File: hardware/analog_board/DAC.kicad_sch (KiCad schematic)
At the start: 120 parts, among them Q1 MMBT3906, Q2 MMBT3906, U3 AD9747BCPZ, U4 OPA695ID, U5 OPA695ID, U6 NE5532

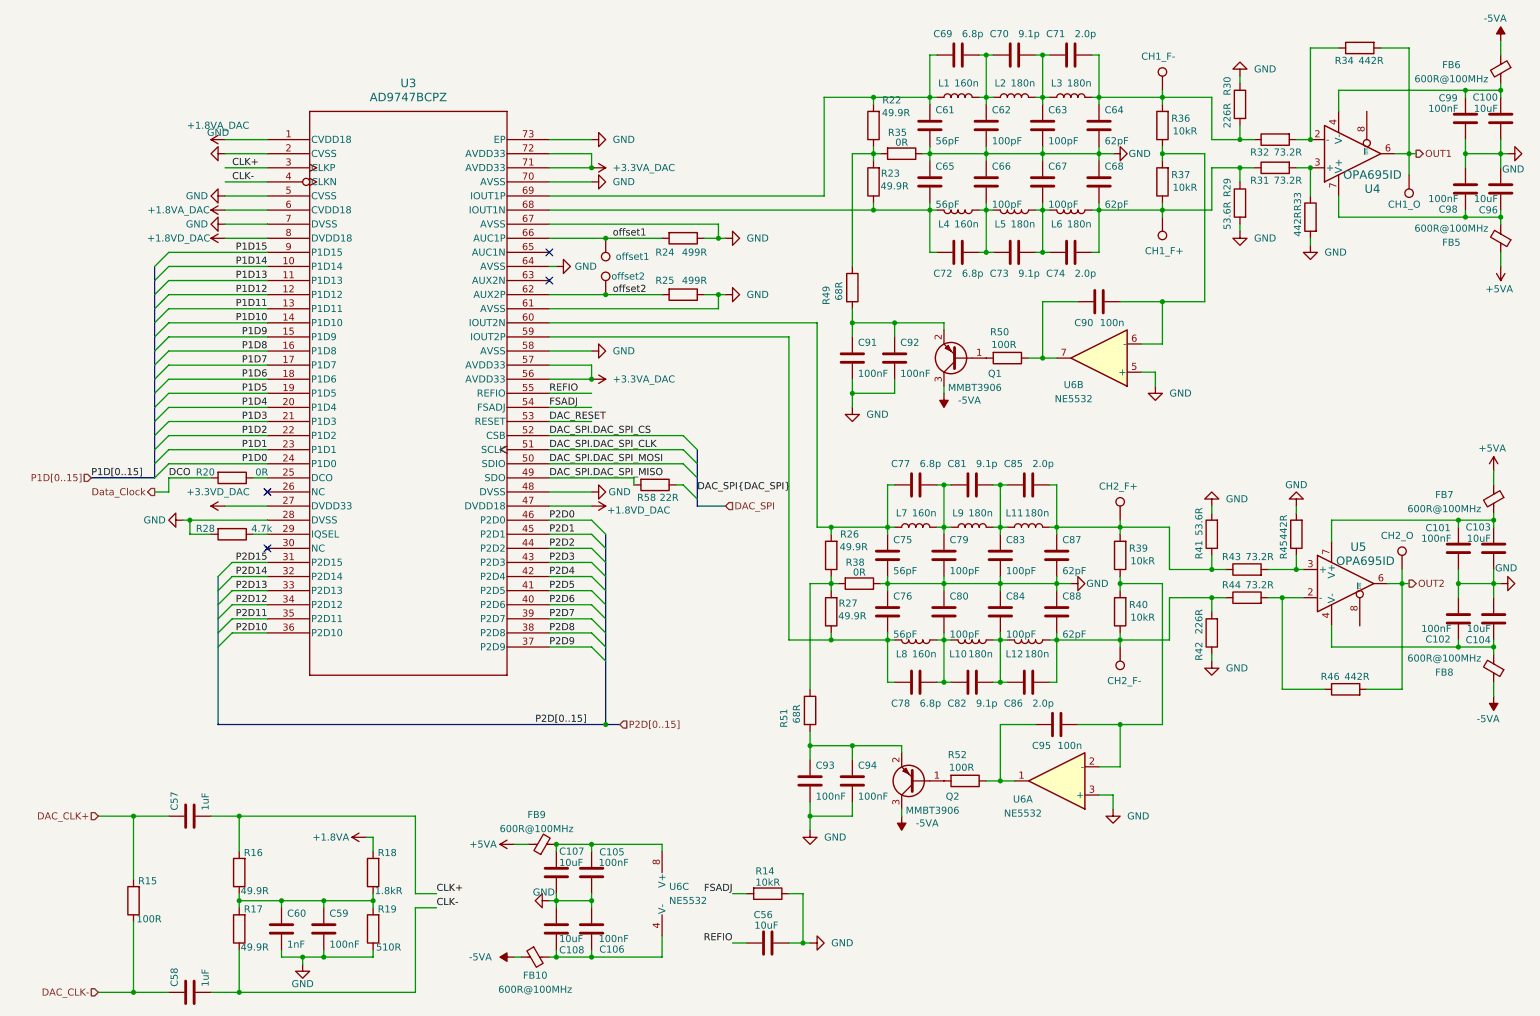
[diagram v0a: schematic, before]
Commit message: feat：根据PCB微调原理图
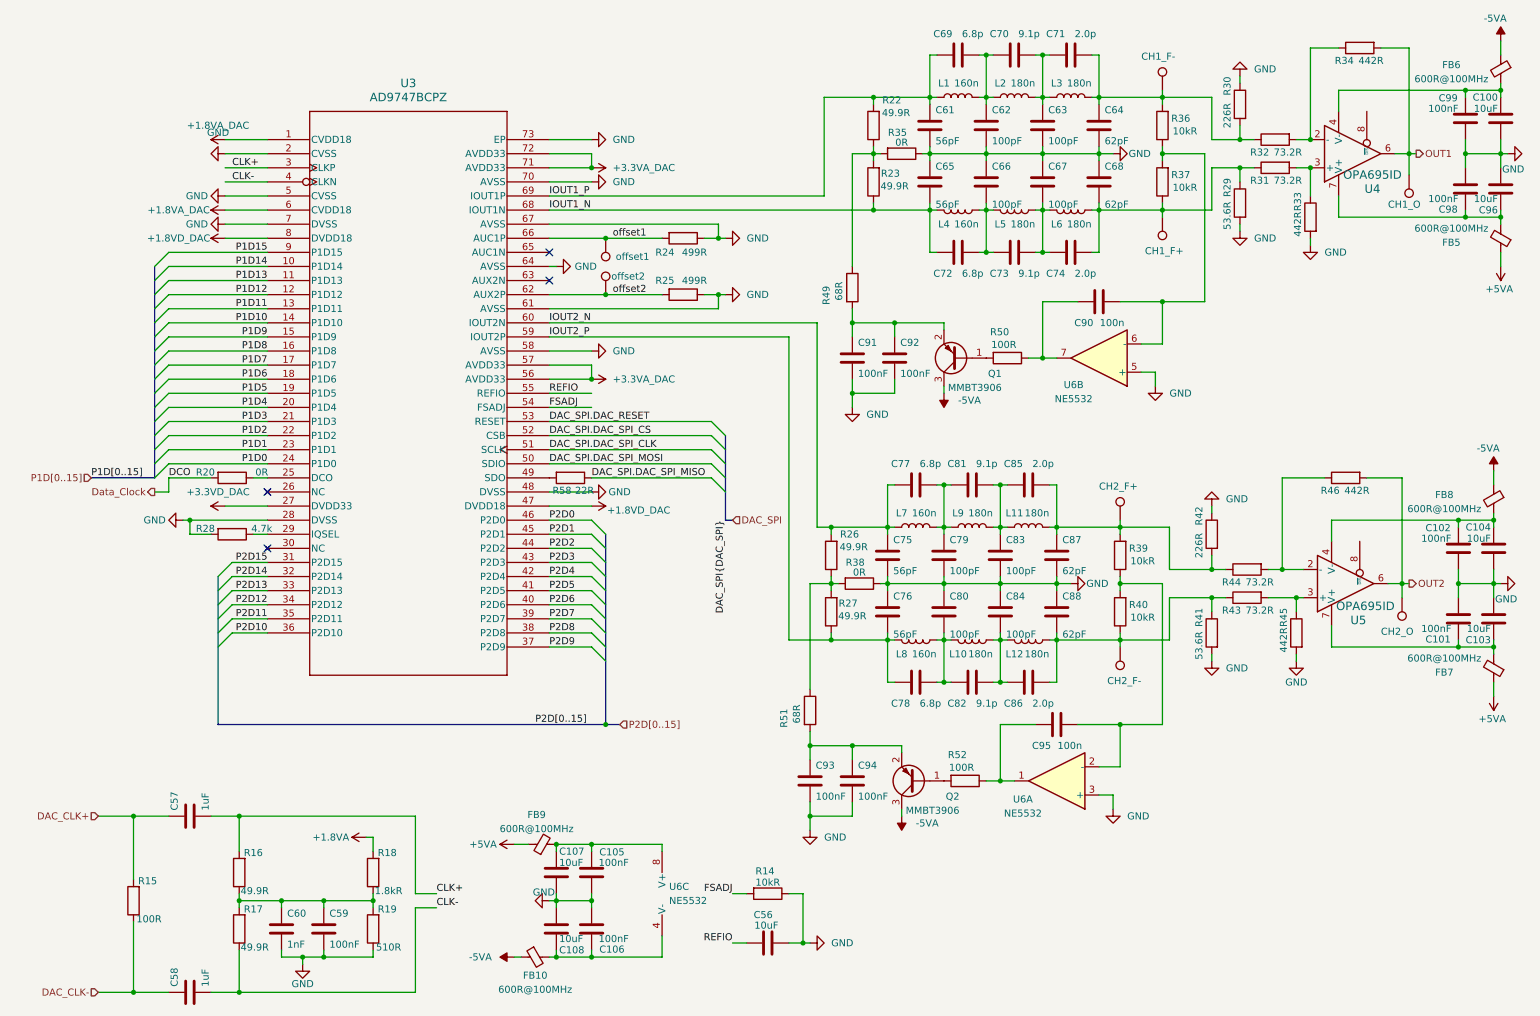
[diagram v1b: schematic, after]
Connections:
- net DAC_SPI.DAC_SPI_MISO: now also R58.1; no longer R58.2, U3.49 (SDO)
- net IOUT2_P: now reaches C76.1, C78.2, L8.1, R27.1, U3.59 (IOUT2P)
- net IOUT2_N: now reaches C75.2, C77.2, L7.1, R26.2, U3.60 (IOUT2N)
- net IOUT1_N: now reaches C65.1, C72.2, L4.1, R23.1, U3.68 (IOUT1N)
- net IOUT1_P: now reaches C61.2, C69.2, L1.1, R22.2, U3.69 (IOUT1P)
- net at C85.1, C87.2, L11.2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: now also R42.2, R44.1; no longer R41.1, R43.1
- net at C86.1, C88.1, L12.2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: now also R41.1, R43.1; no longer R42.2, R44.1
- net DAC_RESET renamed DAC_SPI.DAC_RESET
- new net: R58.2, U3.49 (SDO)
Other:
- moved on the sheet: R58

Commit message: feat：添加平衡铜
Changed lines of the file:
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@@
 		(in_pos_files yes)
 		(dnp no)
-		(fields_autoplaced yes)
 		(property "Reference" "#PWR049"
 			(at 53.34 39.37 0)
@@
 		)
 		(property "Value" "+1.8VA_DAC"
-			(at 48.26 36.83 90)
+			(at 41.148 39.116 90)
 			(show_name no)
 			(do_not_autoplace no)
@@
 		(in_pos_files yes)
 		(dnp no)
-		(fields_autoplaced yes)
 		(property "Reference" "#PWR032"
 			(at 43.18 41.91 0)
@@
 		)
 		(property "Value" "GND"
-			(at 48.26 38.1 90)
+			(at 44.704 41.91 90)
 			(show_name no)
 			(do_not_autoplace no)

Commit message: feat：导出模拟板 BOM
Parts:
- TP1, TP2, TP3, TP4, TP5, TP6, TP7, TP8: now left out of the parts list
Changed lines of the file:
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@@
 		(body_style 1)
 		(exclude_from_sim no)
-		(in_bom yes)
+		(in_bom no)
 		(on_board yes)
 		(in_pos_files yes)
@@
 		(body_style 1)
 		(exclude_from_sim no)
-		(in_bom yes)
+		(in_bom no)
 		(on_board yes)
 		(in_pos_files yes)
@@
 		(body_style 1)
 		(exclude_from_sim no)
-		(in_bom yes)
+		(in_bom no)
 		(on_board yes)
 		(in_pos_files yes)
@@
 		(body_style 1)
 		(exclude_from_sim no)
-		(in_bom yes)
+		(in_bom no)
 		(on_board yes)
 		(in_pos_files yes)
@@
 		(body_style 1)
 		(exclude_from_sim no)
-		(in_bom yes)
+		(in_bom no)
 		(on_board yes)
 		(in_pos_files yes)
@@
 		(body_style 1)
 		(exclude_from_sim no)
-		(in_bom yes)
+		(in_bom no)
 		(on_board yes)
 		(in_pos_files yes)
@@
 		(body_style 1)
 		(exclude_from_sim no)
-		(in_bom yes)
+		(in_bom no)
 		(on_board yes)
 		(in_pos_files yes)
@@
 		(body_style 1)
 		(exclude_from_sim no)
-		(in_bom yes)
+		(in_bom no)
 		(on_board yes)
 		(in_pos_files yes)
